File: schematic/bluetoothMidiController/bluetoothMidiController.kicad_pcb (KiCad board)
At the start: 2 copper layers, 152.9 x 57.2 mm, 26 parts, among them J1 To Feather, SW1 OCT-, SW10 G1, SW11 PWR, SW12 G#1, SW13 A1, SW14 A#1, SW15 B1, SW16 C2, SW17 OPT, SW2 OCT+, SW3 C1, SW4 C#1, SW5 D1, SW6 D#1, SW7 E1, SW8 F1, SW9 F#1, U1 MCP23017_SS

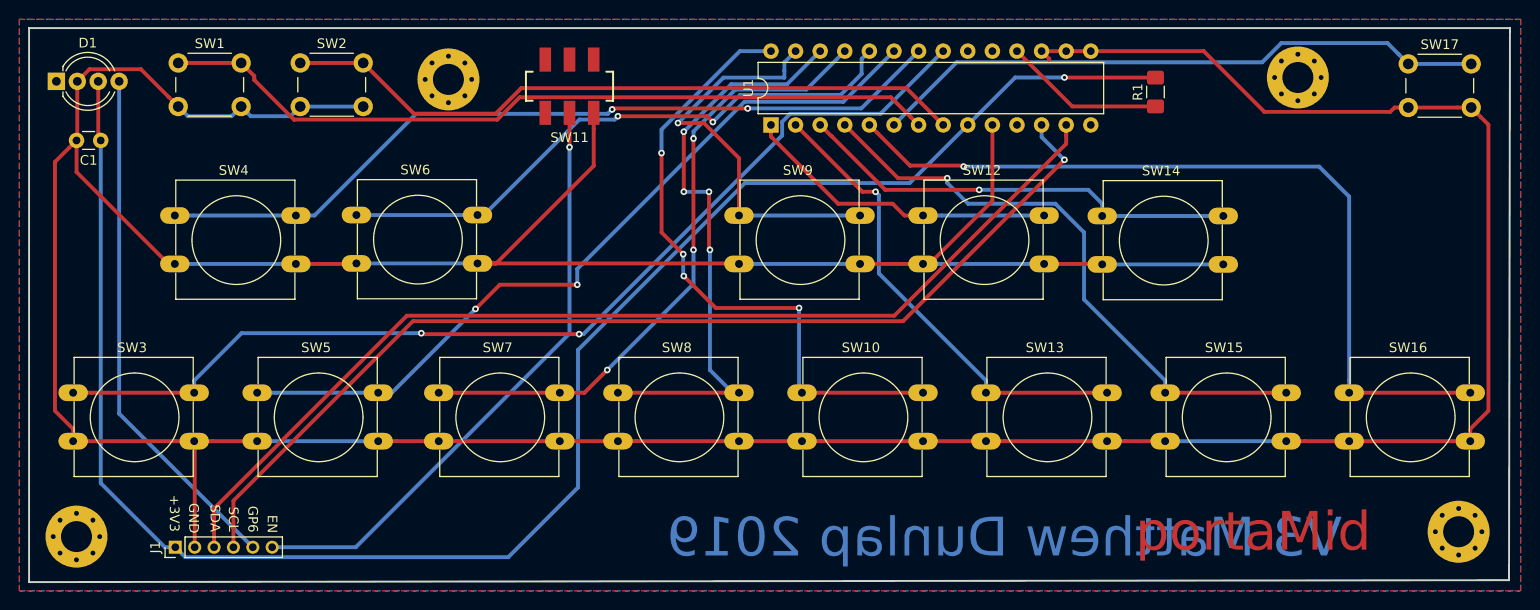
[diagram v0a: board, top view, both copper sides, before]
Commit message: updated PCB to include two 4.7K resisters for I2C bus
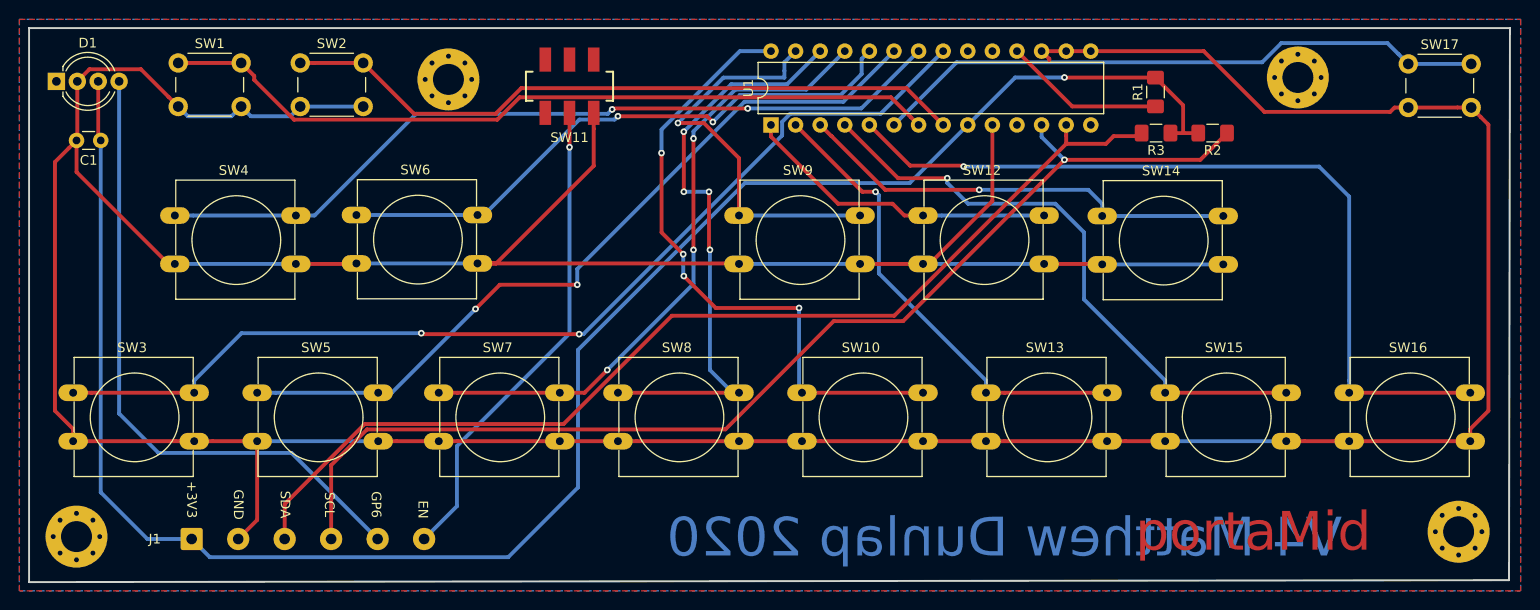
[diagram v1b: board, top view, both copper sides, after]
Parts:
- added R2: 4.7K, Resistor_SMD:R_1206_3216Metric_Pad1.42x1.75mm_HandSolder, F.Cu at (203.2, 78.7)
- added R3: 4.7K, Resistor_SMD:R_1206_3216Metric_Pad1.42x1.75mm_HandSolder, F.Cu at (197.4, 78.7)
- J1: footprint Connector_PinHeader_2.00mm:PinHeader_1x06_P2.00mm_Vertical -> Connector_Wire:SolderWire-0.5sqmm_1x06_P4.8mm_D0.9mm_OD2.3mm
- moved J1 1.89 mm to (97.8, 120.7), turned to 0 degrees
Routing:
- net Net-(D1-Pad4): track 53.8 -> 66.4 mm
- net Net-(J1-Pad6): track 62.6 -> 50.2 mm
- net +3V3: track 182.5 -> 192.8 mm
- net Net-(J1-Pad4): track 109.8 -> 118.9 mm
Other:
- board text added: "V4 Matthew Dunlap 2020"
- board text removed: "V3 Matthew Dunlap 2019"
